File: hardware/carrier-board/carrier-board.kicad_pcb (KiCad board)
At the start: 4 copper layers, 50 x 50 mm, 23 parts, among them J1 DIN41612_02x08_AB_EvenPins, J2 DIN41612_02x08_AB_EvenPins, J3 TC2030, J4 Conn_01x04_Socket, J5 Conn_01x04_Pin, J6 USB_C_Receptacle_USB2.0_16P, SW1 SW_Push, U1 STM32G474RETx, U2 AMS1117-3.3, Y1 Crystal_GND3

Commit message: sch review
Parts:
- added C10: 10uF, Capacitor_SMD:C_0805_2012Metric, F.Cu at (206.6, 116.3)
- added C11: 100nF, Capacitor_SMD:C_0805_2012Metric, F.Cu at (206.6, 119.3)
- added C12: 100nF, Capacitor_SMD:C_0805_2012Metric, F.Cu at (206.6, 122.3)
- added C3: 100nf, Capacitor_SMD:C_0603_1608Metric, F.Cu at (197.5, 125.0)
- added C4: 10uF, Capacitor_SMD:C_0805_2012Metric, F.Cu at (197.7, 116.3)
- added C5: 10uF, Capacitor_SMD:C_0805_2012Metric, F.Cu at (197.7, 119.3)
- added C6: 100nF, Capacitor_SMD:C_0805_2012Metric, F.Cu at (197.7, 122.3)
- added C7: 100nF, Capacitor_SMD:C_0805_2012Metric, F.Cu at (202.1, 116.3)
- added C8: 100nF, Capacitor_SMD:C_0805_2012Metric, F.Cu at (202.1, 119.3)
- added C9: 100nF, Capacitor_SMD:C_0805_2012Metric, F.Cu at (202.1, 122.3)
- added R10: 4.7K, Resistor_SMD:R_0805_2012Metric, F.Cu at (197.7, 107.4)
- added R11: 4.7K, Resistor_SMD:R_0805_2012Metric, F.Cu at (197.7, 110.3)
- added R12: 10k, Resistor_SMD:R_0805_2012Metric, F.Cu at (197.7, 113.3)
- added R8: 5.1k, Resistor_SMD:R_0805_2012Metric, F.Cu at (197.7, 101.5)
- added R9: 5.1k, Resistor_SMD:R_0805_2012Metric, F.Cu at (197.7, 104.4)
- added TP1: TestPoint, TestPoint:TestPoint_Pad_D1.0mm, F.Cu at (135.0, 104.0)
- added TP2: TestPoint, TestPoint:TestPoint_Pad_D1.0mm, F.Cu at (111.0, 124.0)
- added TP3: TestPoint, TestPoint:TestPoint_Pad_D1.0mm, F.Cu at (142.5, 124.8)
- added TP4: TestPoint, TestPoint:TestPoint_Pad_D1.0mm, F.Cu at (142.5, 139.5)
- C1, C2: value C -> 22pf; footprint Capacitor_SMD:C_0603_1608Metric -> Capacitor_SMD:C_0805_2012Metric
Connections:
- J6 pad A5: unconnected-(J6-CC1-PadA5) -> Net-(J6-CC1)
- J6 pad A6: /mcu_core/USB_D- -> unconnected-(J6-D+-PadA6)
- J6 pad B5: unconnected-(J6-CC2-PadB5) -> Net-(J6-CC2)
- J6 pad B6: unconnected-(J6-D+-PadB6) -> /mcu_core/USB_D+
- J6 pad B7: /mcu_core/USB_D+ -> /mcu_core/USB_D-
- R1 pad 2: Net-(R1-Pad2) -> /mcu_core/RESET
- SW1 pad 2: Net-(R1-Pad2) -> /mcu_core/RESET
- U1 pad 10: unconnected-(U1-PC2-Pad10) -> /mcu_core/HWID_2
- U1 pad 11: unconnected-(U1-PC3-Pad11) -> /mcu_core/HWID_3
- U1 pad 12: unconnected-(U1-PA0-Pad12) -> /mcu_core/HWID_A
- U1 pad 13: unconnected-(U1-PA1-Pad13) -> /mcu_core/TRT_GPIO_1
- U1 pad 14: unconnected-(U1-PA2-Pad14) -> /mcu_core/TRT_GPIO_2
- U1 pad 17: unconnected-(U1-PA3-Pad17) -> /mcu_core/TRT_GPIO_3
- U1 pad 18: unconnected-(U1-PA4-Pad18) -> /mcu_core/SPI_CS / PWM
- U1 pad 19: unconnected-(U1-PA5-Pad19) -> /mcu_core/SPI_SCK / PWM
- U1 pad 20: unconnected-(U1-PA6-Pad20) -> /mcu_core/SPI_MISO / PWM
- U1 pad 21: unconnected-(U1-PA7-Pad21) -> /mcu_core/SPI_MOSI / PWM
- U1 pad 42: unconnected-(U1-PA8-Pad42) -> /mcu_core/SDA
- U1 pad 43: unconnected-(U1-PA9-Pad43) -> /mcu_core/SCL
- U1 pad 60: unconnected-(U1-PB7-Pad60) -> Net-(U1-PB7)
- U1 pad 8: unconnected-(U1-PC0-Pad8) -> /mcu_core/HWID_0
- U1 pad 9: unconnected-(U1-PC1-Pad9) -> /mcu_core/HWID_1

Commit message: feat(hardware): finalize schematic, update README and set initial PCB layout
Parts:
- added C13: 100nf, Capacitor_SMD:C_0603_1608Metric, F.Cu at (134.0, 145.5)
- added D1: LED, LED_SMD:LED_0805_2012Metric, F.Cu at (119.0, 136.5)
- added D2: LED, LED_SMD:LED_0805_2012Metric, F.Cu at (135.5, 117.5)
- added D3: 1N5819HW, Diode_SMD:D_SOD-123, F.Cu at (135.0, 136.5)
- added FB1: FerriteBead, Inductor_SMD:L_0805_2012Metric, F.Cu at (124.9, 124.7)
- added J1: Conn_01x02_Pin, Connector_PinHeader_2.54mm:PinHeader_1x02_P2.54mm_Vertical, F.Cu at (141.5, 137.0)
- added Q1: AO3400A, Package_TO_SOT_SMD:SOT-23, F.Cu at (134.5, 140.4)
- added R13: 1k, Resistor_SMD:R_0805_2012Metric, F.Cu at (119.0, 131.0)
- added R14: 470, Resistor_SMD:R_0805_2012Metric, F.Cu at (138.5, 107.5)
- added R15: 10k, Resistor_SMD:R_0805_2012Metric, F.Cu at (129.5, 142.6)
- added R16: 100, Resistor_SMD:R_0805_2012Metric, F.Cu at (129.5, 145.5)
- R10, R11: value 4.7K -> 2.2K
- moved R8 103.3 mm to (104.0, 144.9), turned to 180 degrees
- moved R9 100.9 mm to (104.0, 142.0), turned to 180 degrees
- moved C5 92.9 mm to (106.5, 137.0)
- moved C4 91.7 mm to (107.0, 129.5)
- moved C12 85.2 mm to (121.5, 125.0), turned to 90 degrees
- moved C11 82.7 mm to (124.5, 129.5), turned to 90 degrees
- moved C6 80.9 mm to (116.8, 120.0), turned to 180 degrees
- moved R12 80.5 mm to (118.0, 124.9), turned to 90 degrees
- moved C10 78.9 mm to (129.0, 130.4), turned to 90 degrees
- moved C3 73.3 mm to (126.0, 141.5), turned to 90 degrees
- moved C9 73.2 mm to (129.0, 126.0), turned to -90 degrees
- moved C8 67.0 mm to (135.3, 114.5)
- moved C7 66.9 mm to (135.4, 111.5)
- moved R10 61.3 mm to (141.5, 132.0)
- moved R11 59.5 mm to (141.5, 130.0)
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- renumbered J1 to J2
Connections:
- J2 pad 1: (no net) -> /mcu_core/SPI_CS / PWM
- J2 pad 10: (no net) -> /mcu_core/TRT_GPIO_2
- J2 pad 11: (no net) -> /mcu_core/HWID_1
- J2 pad 12: (no net) -> /mcu_core/SDA
- J2 pad 13: (no net) -> /mcu_core/HWID_2
- J2 pad 14: (no net) -> /mcu_core/SCL
- J2 pad 15: (no net) -> /mcu_core/HWID_3
- J2 pad 16: (no net) -> /mcu_core/TRT_GPIO_3
- J2 pad 2: (no net) -> GND
- J2 pad 3: (no net) -> /mcu_core/SPI_MOSI / PWM
- J2 pad 4: (no net) -> +5V
- J2 pad 5: (no net) -> /mcu_core/SPI_MISO / PWM
- J2 pad 6: (no net) -> /mcu_core/TRT_GPIO_1
- J2 pad 7: (no net) -> /mcu_core/SPI_SCK / PWM
- J2 pad 8: (no net) -> +3.3V
- J2 pad 9: (no net) -> /mcu_core/HWID_0
- R10 pad 1: +3.3V -> /mcu_core/I2C_PU_EN
- R11 pad 1: +3.3V -> /mcu_core/I2C_PU_EN
- U1 pad 1: unconnected-(U1-VBAT-Pad1) -> +3.3V
- U1 pad 14: /mcu_core/TRT_GPIO_2 -> unconnected-(U1-PA2-Pad14)
- U1 pad 17: /mcu_core/TRT_GPIO_3 -> unconnected-(U1-PA3-Pad17)
- U1 pad 18: /mcu_core/SPI_CS / PWM -> /mcu_core/TRT_GPIO_2
- U1 pad 24: unconnected-(U1-PB0-Pad24) -> /mcu_core/TRT_GPIO_3
- U1 pad 32: unconnected-(U1-VDD-Pad32) -> +3.3V
- U1 pad 4: unconnected-(U1-PC15-Pad4) -> /mcu_core/I2C_PU_EN
- U1 pad 42: /mcu_core/SDA -> unconnected-(U1-PA8-Pad42)
- U1 pad 43: /mcu_core/SCL -> unconnected-(U1-PA9-Pad43)
- U1 pad 48: unconnected-(U1-VDD-Pad48) -> +3.3V
- U1 pad 57: unconnected-(U1-PB4-Pad57) -> /mcu_core/Vm_out
- U1 pad 59: unconnected-(U1-PB6-Pad59) -> /mcu_core/SPI_CS / PWM
- U1 pad 61: unconnected-(U1-PB8-Pad61) -> /mcu_core/SCL
- U1 pad 62: unconnected-(U1-PB9-Pad62) -> /mcu_core/SDA
- U1 pad 64: unconnected-(U1-VDD-Pad64) -> +3.3V

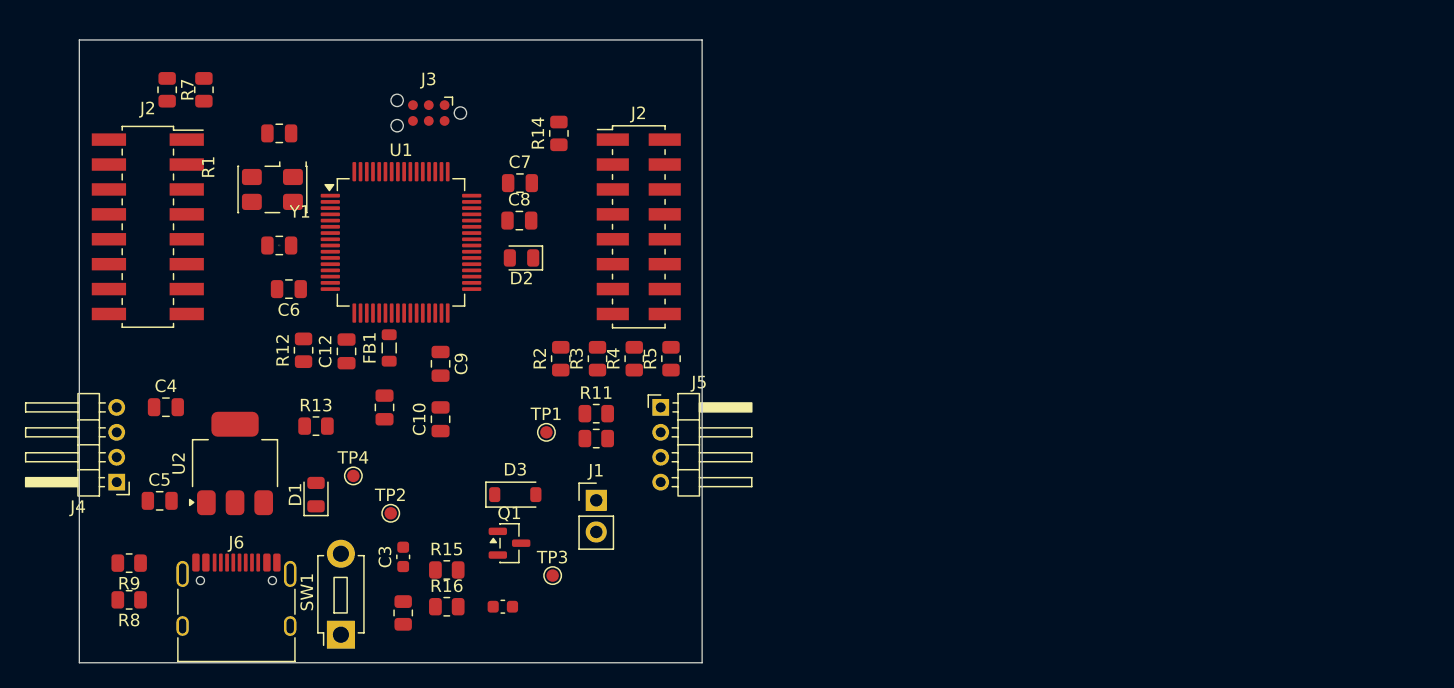
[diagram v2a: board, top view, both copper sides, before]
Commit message: pcb placement
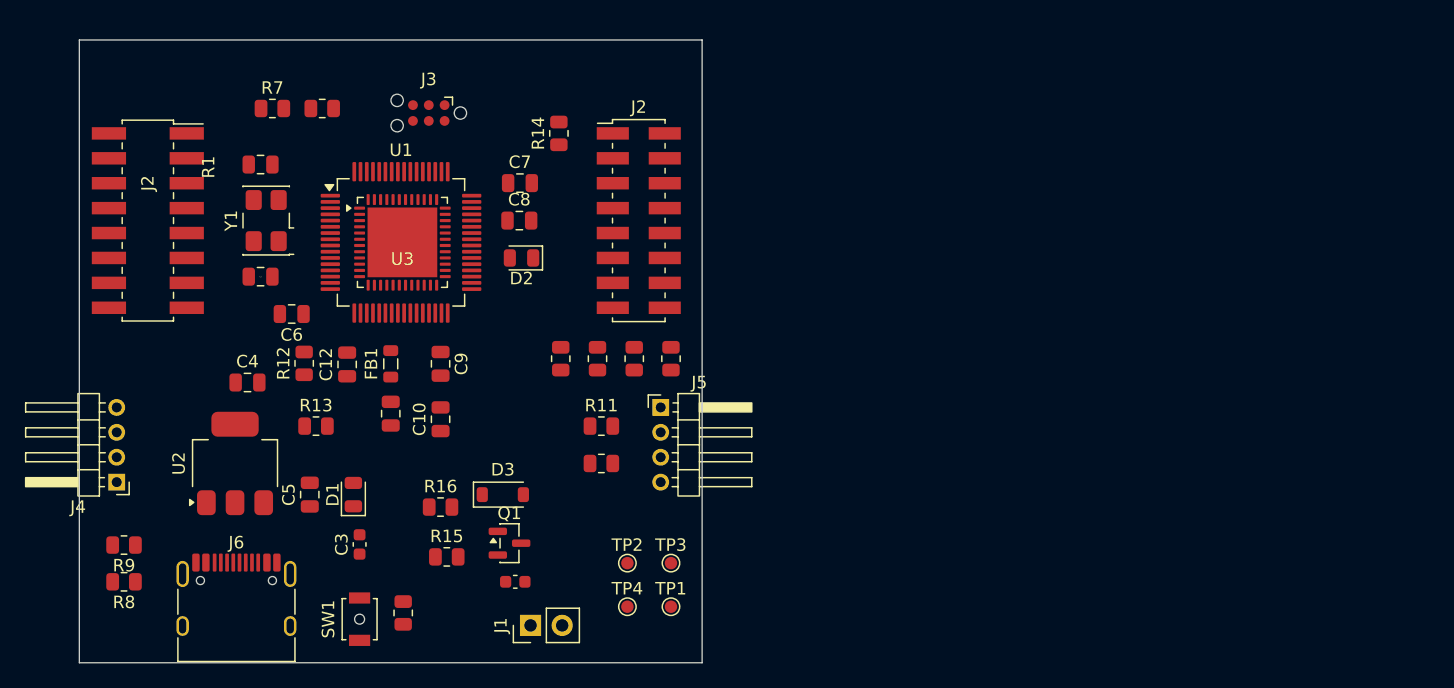
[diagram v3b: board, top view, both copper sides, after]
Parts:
- added U3: STM32F411CEUx, Package_DFN_QFN:QFN-48-1EP_7x7mm_P0.5mm_EP5.6x5.6mm, F.Cu at (125.9, 116.2)
- SW1: footprint Button_Switch_THT:SW_PUSH_1P1T_6x3.5mm_H5.0_APEM_MJTP1250 -> Button_Switch_SMD:SW_SPST_B3U-1000P-B
- moved TP4 24.4 mm to (144.0, 145.5)
- moved TP2 19.4 mm to (144.0, 142.0)
- moved TP1 17.2 mm to (147.5, 145.5)
- moved C5 12.1 mm to (118.5, 136.5), turned to 90 degrees
- moved J1 11.3 mm to (136.2, 147.0), turned to 90 degrees
- moved R6 9.62 mm to (119.5, 105.5), turned to 0 degrees
- moved TP3 9.55 mm to (147.5, 142.0)
- moved R7 8.58 mm to (115.5, 105.5), turned to 0 degrees
- moved R16 8.02 mm to (129.0, 137.5)
- moved C4 6.84 mm to (113.5, 127.5)
- moved C3 3.64 mm to (122.5, 140.5)
- moved D1 3.00 mm to (122.0, 136.5)
- moved C1 2.92 mm to (114.5, 110.0)
- moved C2 2.92 mm to (114.5, 119.0)
- moved Y1 2.55 mm to (115.0, 114.5), turned to 90 degrees
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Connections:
- Y1 pad 1: Net-(U1-PF0) -> Net-(U1-PF1)
- Y1 pad 2: Net-(U1-PF1) -> Net-(U1-PF0)
